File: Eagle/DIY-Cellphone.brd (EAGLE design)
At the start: 77.5 x 44.5 mm, 39 parts, among them IC1 MEGA1284, J1 ISP, U1 MCP73831, U7 M10_HDWITHOUT_EXCLUSION, X1 BU-SMA-V, X3 CCM03-3002 R102

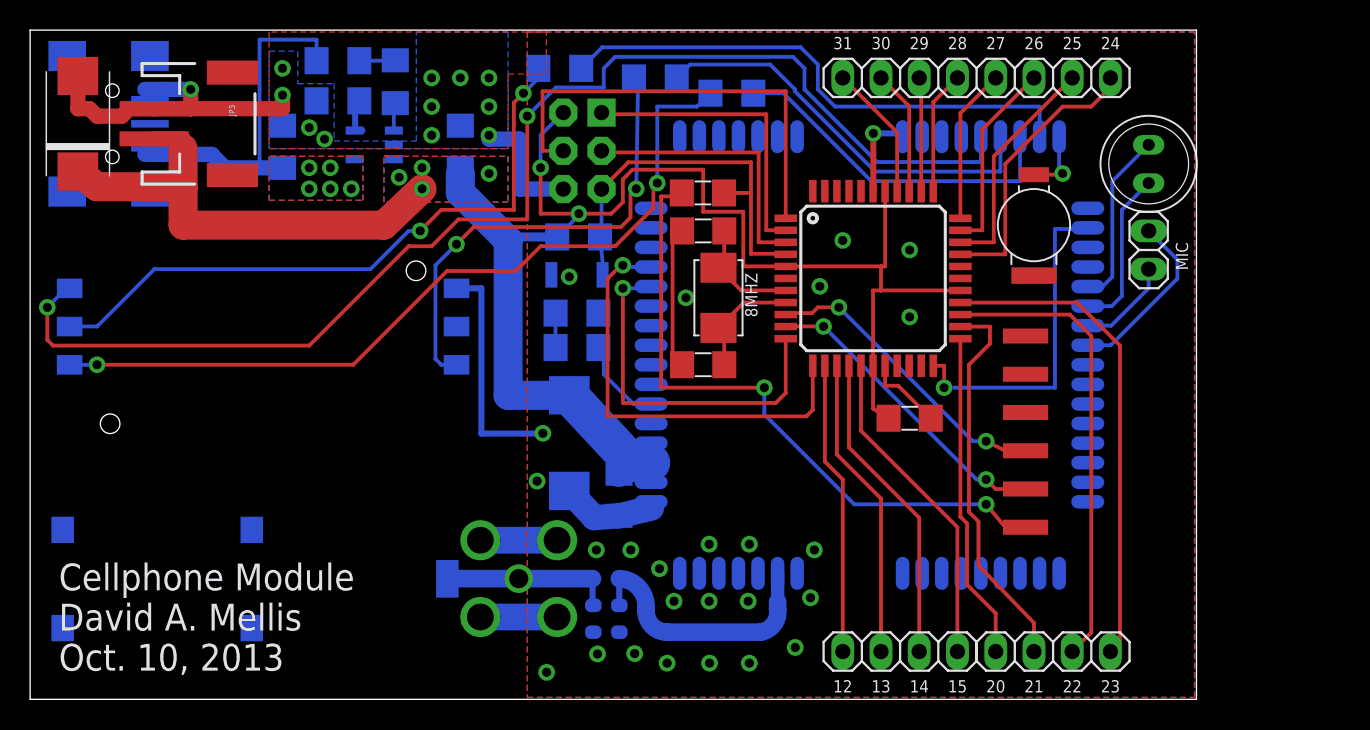
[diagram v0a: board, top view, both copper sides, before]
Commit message: Add thermals and increase isolate on ground planes for easier soldering.
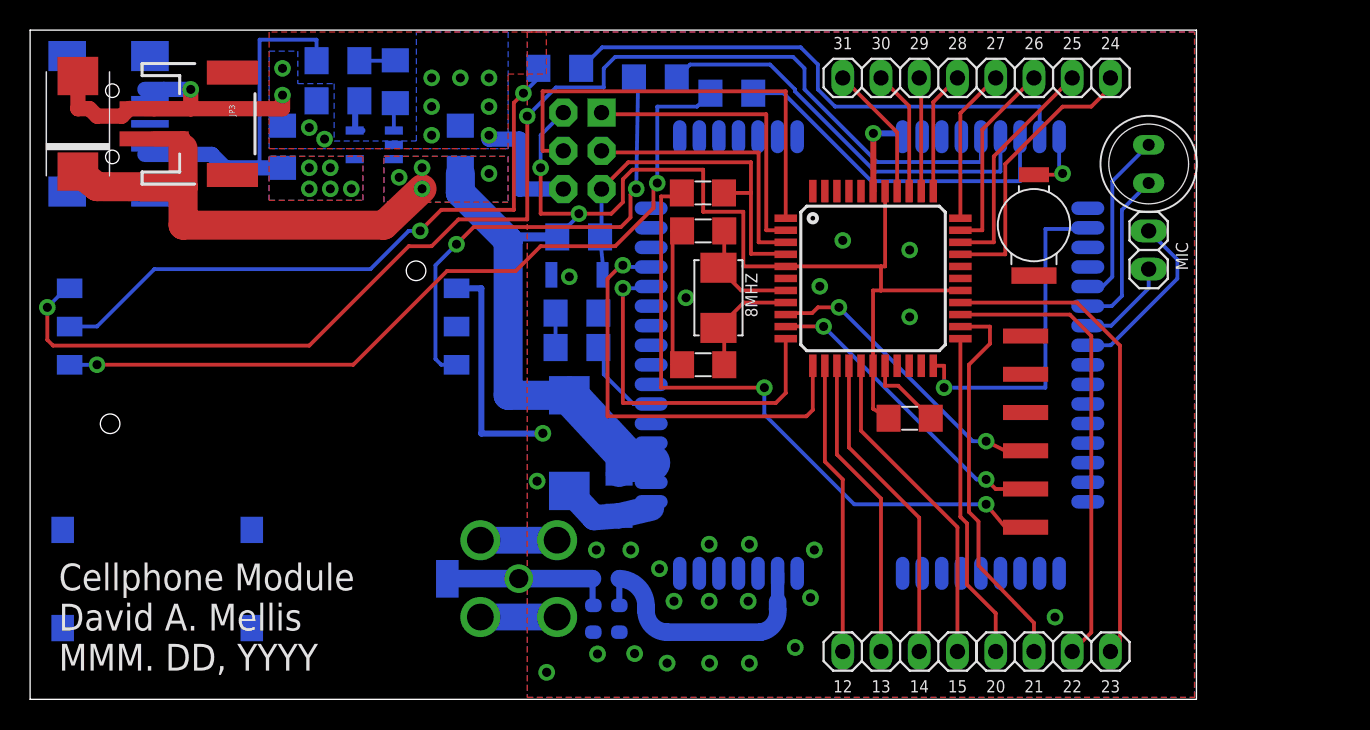
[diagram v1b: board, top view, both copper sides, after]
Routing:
- net GND: vias 38 -> 39
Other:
- board text added: "Cellphone Module David A. Mellis MMM. DD, YYYY"
- board text removed: "Cellphone Module David A. Mellis Oct. 10, 2013"
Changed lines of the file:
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@@
 <grid distance="25" unitdist="mil" unit="mil" style="dots" multiple="2" display="no" altdistance="5" altunitdist="mil" altunit="mil"/>
 <layers>
-<layer number="1" name="Top" color="4" fill="1" visible="yes" active="yes"/>
+<layer number="1" name="Top" color="4" fill="1" visible="no" active="yes"/>
 <layer number="16" name="Bottom" color="1" fill="1" visible="yes" active="yes"/>
 <layer number="17" name="Pads" color="2" fill="1" visible="yes" active="yes"/>
@@
 <layer number="19" name="Unrouted" color="6" fill="1" visible="yes" active="yes"/>
 <layer number="20" name="Dimension" color="15" fill="1" visible="yes" active="yes"/>
-<layer number="21" name="tPlace" color="7" fill="1" visible="yes" active="yes"/>
+<layer number="21" name="tPlace" color="7" fill="1" visible="no" active="yes"/>
 <layer number="22" name="bPlace" color="5" fill="1" visible="yes" active="yes"/>
-<layer number="23" name="tOrigins" color="15" fill="1" visible="yes" active="yes"/>
+<layer number="23" name="tOrigins" color="15" fill="1" visible="no" active="yes"/>
 <layer number="24" name="bOrigins" color="15" fill="1" visible="yes" active="yes"/>
-<layer number="25" name="tNames" color="7" fill="1" visible="yes" active="yes"/>
+<layer number="25" name="tNames" color="7" fill="1" visible="no" active="yes"/>
 <layer number="26" name="bNames" color="6" fill="1" visible="yes" active="yes"/>
-<layer number="27" name="tValues" color="7" fill="1" visible="yes" active="yes"/>
+<layer number="27" name="tValues" color="7" fill="1" visible="no" active="yes"/>
 <layer number="28" name="bValues" color="7" fill="1" visible="yes" active="yes"/>
 <layer number="29" name="tStop" color="2" fill="3" visible="no" active="yes"/>
@@
 <layer number="40" name="bKeepout" color="1" fill="11" visible="no" active="yes"/>
 <layer number="41" name="tRestrict" color="14" fill="11" visible="no" active="yes"/>
-<layer number="42" name="bRestrict" color="1" fill="10" visible="no" active="yes"/>
+<layer number="42" name="bRestrict" color="1" fill="10" visible="yes" active="yes"/>
 <layer number="43" name="vRestrict" color="2" fill="10" visible="no" active="yes"/>
 <layer number="44" name="Drills" color="7" fill="1" visible="no" active="yes"/>
@@
 <text x="1.905" y="1.905" size="1.778" layer="25" font="fixed">Cellphone Module
 David A. Mellis
-Oct. 10, 2013</text>
+MMM. DD, YYYY</text>
 <text x="71.12" y="43.18" size="0.8128" layer="25" font="fixed">24</text>
 <text x="68.58" y="43.18" size="0.8128" layer="25" font="fixed">25</text>
@@
 <text x="57.15" y="43.18" size="0.8128" layer="26" font="fixed" rot="MR0">30</text>
 <text x="54.61" y="43.18" size="0.8128" layer="26" font="fixed" rot="MR0">31</text>
+<rectangle x1="34.671" y1="12.954" x2="40.259" y2="18.923" layer="42"/>
 </plain>
 <attributes>
@@
 <wire x1="10.668" y1="39.227" x2="16.764" y2="39.227" width="1.016" layer="1"/>
 <wire x1="16.764" y1="39.227" x2="16.764" y2="40.132" width="1.016" layer="1"/>
-<polygon width="0.254" layer="16" isolate="0.254" thermals="no">
+<polygon width="0.254" layer="16" isolate="0.4064">
 <vertex x="77.343" y="44.323"/>
 <vertex x="33.02" y="44.323"/>
@@
 <vertex x="77.343" y="0.127"/>
 </polygon>
-<polygon width="0.254" layer="1" isolate="0.254" thermals="no">
+<polygon width="0.254" layer="1" isolate="0.4064">
 <vertex x="77.343" y="44.323"/>
 <vertex x="33.02" y="44.323"/>
@@
 <wire x1="42.672" y1="22.225" x2="43.304" y2="22.225" width="0.254" layer="1"/>
 <via x="43.561" y="26.67" extent="1-16" drill="0.6"/>
+<via x="68.072" y="5.461" extent="1-16" drill="0.6"/>
 </signal>
 <signal name="DISP_DATA">
@@
 <wire x1="60.706" y1="22.156" x2="60.706" y2="20.701" width="0.254" layer="1"/>
 <via x="60.706" y="20.701" extent="1-16" drill="0.6"/>
-<wire x1="60.706" y1="20.701" x2="68.072" y2="20.701" width="0.254" layer="16"/>
-<wire x1="68.072" y1="20.701" x2="68.072" y2="31.242" width="0.254" layer="16"/>
-<wire x1="68.072" y1="31.242" x2="70.25" y2="31.242" width="0.254" layer="16"/>
+<wire x1="60.706" y1="20.701" x2="67.437" y2="20.701" width="0.254" layer="16"/>
+<wire x1="67.437" y1="20.701" x2="67.437" y2="31.242" width="0.254" layer="16"/>
+<wire x1="67.437" y1="31.242" x2="70.25" y2="31.242" width="0.254" layer="16"/>
 <wire x1="70.25" y1="31.242" x2="70.25" y2="31.319" width="0.254" layer="16"/>
 </signal>

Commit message: Break out I2C and SPI pins.
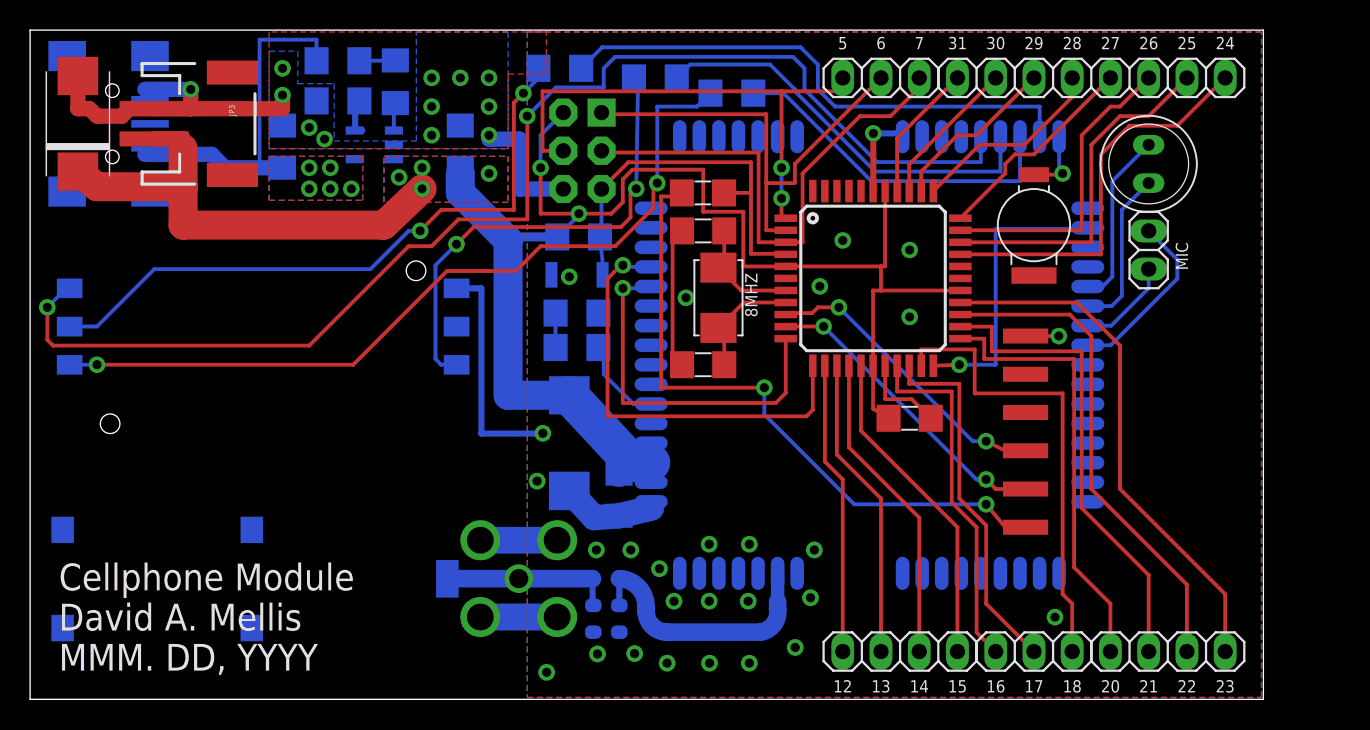
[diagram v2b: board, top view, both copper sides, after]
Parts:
- added JP4, JP6: (no value), pinhead:1X03
- moved JP1 7.62 mm to (75.6, 3.17)
- moved JP2 7.62 mm to (70.5, 41.3)
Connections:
- net MISO: now also JP6.2
- net MOSI: now also JP6.1
- net PC0: now also JP4.1
- net PC1: now also JP4.2
- net PC2: now also JP4.3
- net SCK: now also JP6.3
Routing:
- net PC2: track 0.00 -> 30.8 mm
- net PC1: track 0.00 -> 24.4 mm
- net PC0: track 0.00 -> 23.8 mm
- net SCK: track 18.3 -> 34.7 mm
- net MISO: track 20.1 -> 31.3 mm
- net PA6: track 15.3 -> 23.4 mm
- net PA7: track 18.7 -> 26.3 mm
- net PC4: track 21.8 -> 29.3 mm
- net PA5: track 13.0 -> 20.4 mm
- net PC5: track 25.9 -> 31.5 mm
- net MOSI: track 29.9 -> 34.8 mm, vias 0 -> 2
- net PA3: track 8.18 -> 13.1 mm
- net PA4: track 10.3 -> 14.2 mm
- net PA2: track 7.57 -> 11.4 mm
- net PWRKEY: track 22.3 -> 19.4 mm
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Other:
- board size 77.5 x 44.5 mm -> 81.9 x 44.5 mm
- board text added: "16"
- board text added: "17"
- board text added: "18"
- board text added: "5"
- board text added: "6"
- board text added: "7"
- board text added: "B"
- board text added: "G"

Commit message: Break out power and ground.
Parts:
- added JP8, JP9: (no value), pinhead:1X02
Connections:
- net GND: now also JP8.2, JP9.2
- net VCC: now also JP8.1, JP9.1
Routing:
- net VCC: track 128.7 -> 187.0 mm
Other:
- board size 81.9 x 44.5 mm -> 87 x 44.5 mm
- board text added: "GND"
- board text added: "VCC"
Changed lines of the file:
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@@
 <plain>
 <rectangle x1="0.594" y1="0.697" x2="51.594" y2="34.697" layer="51" rot="R180"/>
-<wire x1="0" y1="44.45" x2="81.915" y2="44.45" width="0" layer="20"/>
-<wire x1="81.915" y1="44.45" x2="81.915" y2="0" width="0" layer="20"/>
-<wire x1="81.915" y1="0" x2="0" y2="0" width="0" layer="20"/>
+<wire x1="0" y1="44.45" x2="86.995" y2="44.45" width="0" layer="20"/>
+<wire x1="86.995" y1="44.45" x2="86.995" y2="0" width="0" layer="20"/>
+<wire x1="86.995" y1="0" x2="0" y2="0" width="0" layer="20"/>
 <wire x1="0" y1="0" x2="0" y2="44.45" width="0" layer="20"/>
 <text x="1.905" y="1.905" size="1.778" layer="25" font="fixed">Cellphone Module
@@
 <text x="57.15" y="43.18" size="0.8128" layer="26" font="fixed" rot="MR0"> 6</text>
 <text x="54.61" y="43.18" size="0.8128" layer="26" font="fixed" rot="MR0"> 5</text>
+<text x="81.28" y="1.27" size="0.8128" layer="25" font="fixed" align="top-left">VCC</text>
+<text x="81.28" y="43.18" size="0.8128" layer="25" font="fixed">VCC</text>
+<text x="83.82" y="43.18" size="0.8128" layer="25" font="fixed">GND</text>
+<text x="83.82" y="1.27" size="0.8128" layer="25" font="fixed" align="top-left">GND</text>
+<text x="82.55" y="43.18" size="0.8128" layer="26" font="fixed" rot="MR0">VCC</text>
+<text x="85.09" y="43.18" size="0.8128" layer="26" font="fixed" rot="MR0">GND</text>
+<text x="82.55" y="1.27" size="0.8128" layer="26" font="fixed" rot="MR0" align="top-left">VCC</text>
+<text x="85.09" y="1.27" size="0.8128" layer="26" font="fixed" rot="MR0" align="top-left">GND</text>
 </plain>
 <attributes>
@@
 <attribute name="VALUE" x="52.705" y="38.1" size="1.27" layer="27"/>
 </element>
+<element name="JP8" library="pinhead" package="1X02" value="" x="83.185" y="3.175" smashed="yes">
+<attribute name="VALUE" x="80.645" y="0" size="1.27" layer="27"/>
+</element>
+<element name="JP9" library="pinhead" package="1X02" value="" x="83.185" y="41.275" smashed="yes">
+<attribute name="VALUE" x="80.645" y="38.1" size="1.27" layer="27"/>
+</element>
 </elements>
 <signals>
@@
 <wire x1="33.909" y1="35.306" x2="33.909" y2="37.468" width="0.254" layer="16"/>
 <wire x1="33.909" y1="37.468" x2="35.414" y2="38.973" width="0.254" layer="16"/>
+<contactref element="JP8" pad="1"/>
+<contactref element="JP9" pad="1"/>
+<wire x1="61.788" y1="27.156" x2="81.915" y2="27.156" width="0.254" layer="1"/>
+<wire x1="81.915" y1="27.156" x2="81.915" y2="27.305" width="0.254" layer="1"/>
+<wire x1="81.915" y1="27.305" x2="81.915" y2="41.275" width="0.254" layer="1"/>
+<wire x1="81.915" y1="3.175" x2="81.915" y2="27.156" width="0.254" layer="1"/>
 </signal>
 <signal name="ANT" class="4">
@@
 <wire x1="16.764" y1="39.227" x2="16.764" y2="40.132" width="1.016" layer="1"/>
 <polygon width="0.254" layer="16" isolate="0.4064">
-<vertex x="81.788" y="44.323"/>
+<vertex x="86.868" y="44.323"/>
 <vertex x="33.02" y="44.323"/>
 <vertex x="33.02" y="0.127"/>
-<vertex x="81.788" y="0.127"/>
+<vertex x="86.868" y="0.127"/>
 </polygon>
 <polygon width="0.254" layer="1" isolate="0.4064">
-<vertex x="81.788" y="44.323"/>
+<vertex x="86.868" y="44.323"/>
 <vertex x="33.02" y="44.323"/>
 <vertex x="33.02" y="0.127"/>
-<vertex x="81.788" y="0.127"/>
+<vertex x="86.868" y="0.127"/>
 </polygon>
 <wire x1="8.238" y1="39.227" x2="10.668" y2="39.227" width="1.016" layer="1"/>
@@
 <wire x1="66.12" y1="24.13" x2="68.326" y2="24.13" width="0.254" layer="1"/>
 <via x="68.326" y="24.13" extent="1-16" drill="0.6"/>
+<contactref element="JP8" pad="2"/>
+<contactref element="JP9" pad="2"/>
 </signal>
 <signal name="DISP_DATA">
@@
 </signal>
 </signals>
-<errors>
-</errors>
 </board>
 </drawing>
